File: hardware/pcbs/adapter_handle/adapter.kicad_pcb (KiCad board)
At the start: 2 copper layers, 7.5 x 7.5 mm, 2 parts, among them J2 XLR4

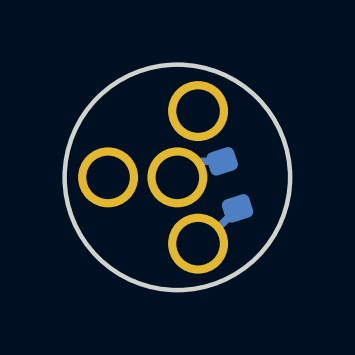
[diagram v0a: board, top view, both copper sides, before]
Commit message: feat: update to 5-pin XLR for sleep
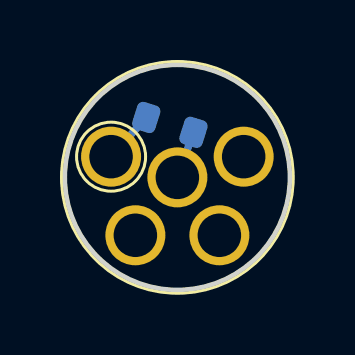
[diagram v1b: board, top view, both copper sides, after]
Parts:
- removed J2: XLR4, connector_audio:MiniXLR-4_Rean_RT4MPR
- added J1: XLR5, connector_audio:MiniXLR-5_Rean_RT5MPR, F.Cu at (139.8, 105.0)
- moved R1 2.83 mm to (139.5, 103.2), turned to 162.5 degrees
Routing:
- net unconnected-(J1-P3-Pad3): track 0.00 -> 1.33 mm
- net /GND: track 2.99 -> 1.76 mm
- net /DET: track 2.27 -> 1.59 mm

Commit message: feat: hw v7a
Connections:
- net /GND renamed /BLUE
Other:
- board text added: "af 25"
- board text added: "v7a"
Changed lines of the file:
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@@
 	(paper "A4")
 	(title_block
-		(title "MiniXLR adapter")
-		(date "2025-08-18")
-		(rev "6c")
+		(title "MiniXLR adapter (handle)")
+		(date "2025-11-10")
+		(rev "7a")
 		(company "elagil")
 	)
@@
 	(net 0 "")
 	(net 1 "/DET")
-	(net 2 "/GND")
+	(net 2 "/BLUE")
 	(net 3 "unconnected-(J1-P3-Pad4)")
 	(net 4 "unconnected-(J1-P3-Pad3)")
@@
 			(layers "*.Cu" "*.Mask")
 			(remove_unused_layers no)
-			(net 2 "/GND")
+			(net 2 "/BLUE")
 			(pinfunction "P1")
 			(pintype "passive")
@@
 			(layers "B.Cu" "B.Mask" "B.Paste")
 			(roundrect_rratio 0.25)
-			(net 2 "/GND")
+			(net 2 "/BLUE")
 			(pintype "passive")
 		)
@@
 		(layer "Edge.Cuts")
 	)
+	(gr_text "af 25"
+		(at 137.5 103 -0)
+		(layer "F.SilkS")
+		(effects
+			(font
+				(size 1 1)
+				(thickness 0.15)
+			)
+			(justify left bottom)
+		)
+	)
+	(gr_text "v7a"
+		(at 141.5 103.125 342.5)
+		(layer "B.SilkS")
+		(effects
+			(font
+				(size 1 1)
+				(thickness 0.15)
+			)
+			(justify left bottom mirror)
+		)
+	)
 	(segment
